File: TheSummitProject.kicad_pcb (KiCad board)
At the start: 4 copper layers, 70 x 65 mm, 81 parts, among them IC1 STM32U5F7VJT6, J1 Cortex SWD, J4 Screen FPC, J5 Micro_SD_Card_Det1, Q1 NMOS, SW1 SW_SPDT, SW2 PWR_BTN, U1 NPM1300-CAAA-R, U2 USBLC6-2SC6, U3 USBLC6-2SC6, Y1 16Mhz, Y2 32.768Khz

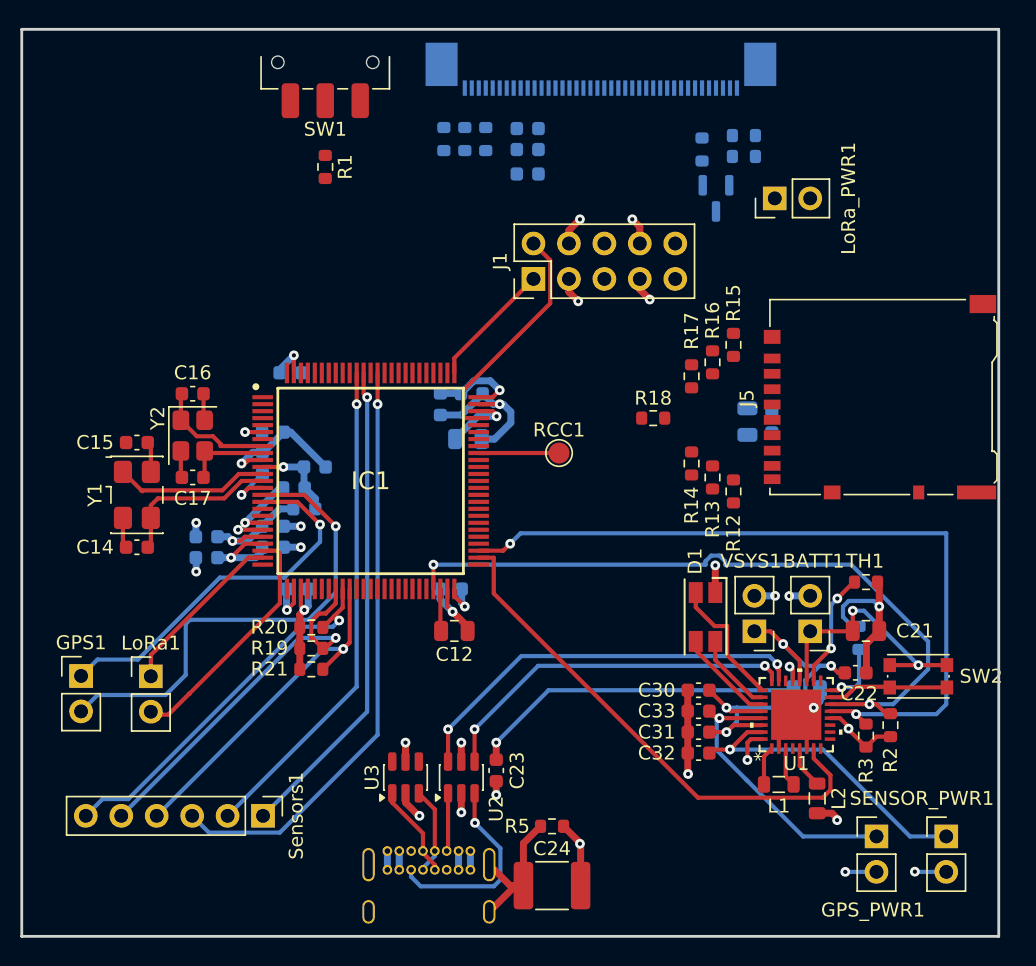
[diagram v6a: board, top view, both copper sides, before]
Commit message: added 90% pcb traces
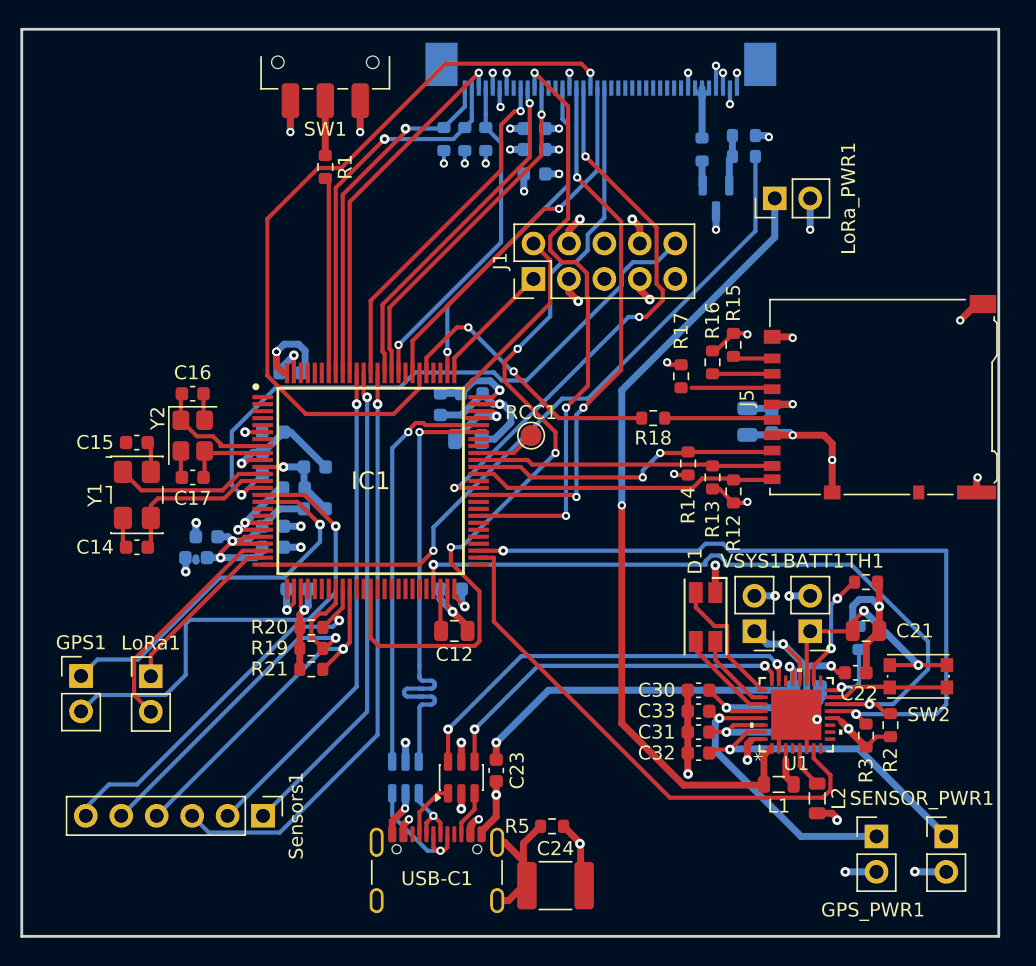
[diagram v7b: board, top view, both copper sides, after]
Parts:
- U3: moved to B.Cu
- USB-C1: footprint Connector_USB:USB_C_Receptacle_GCT_USB4085 -> Connector_USB:USB_C_Receptacle_GCT_USB4105-xx-A_16P_TopMnt_Horizontal; moved to F.Cu
- moved USB-C1 3.45 mm to (154.8, 129.5), turned to 0 degrees
- moved RCC1 2.36 mm to (161.5, 97.2)
- moved C10 0.75 mm to (137.5, 106.0)
- moved FB1 0.75 mm to (146.0, 102.5)
- moved R17 0.75 mm to (172.2, 93.0)
- moved C25 0.50 mm to (161.8, 76.8)
- moved C26 0.50 mm to (161.8, 75.2)
- moved C27 0.50 mm to (161.8, 78.5)
- moved C24 0.25 mm to (163.2, 129.5)
- moved R14 0.25 mm to (172.8, 99.2)
- turned R18 to 180 degrees
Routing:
- net +3.3V_DP_LORA: track 2.81 -> 67.7 mm, vias 0 -> 11
- net LCD_D4: track 0.00 -> 60.8 mm, vias 0 -> 3
- net LCD_D2: track 0.00 -> 54.3 mm, vias 0 -> 1
- net LCD_PWM: track 0.00 -> 51.5 mm, vias 0 -> 1
- net /MCU/NRST: track 3.84 -> 47.0 mm
- net LCD_RS: track 0.00 -> 43.0 mm, vias 0 -> 3
- net LCD_D1: track 0.00 -> 39.8 mm, vias 0 -> 3
- net LCD_D0: track 0.00 -> 39.0 mm, vias 0 -> 3
- net Net-(IC1-USB_OTG_HS_DM): track 0.00 -> 33.6 mm, vias 0 -> 1
- net Net-(IC1-USB_OTG_HS_DP): track 0.00 -> 29.5 mm, vias 0 -> 1
- net CTP_SDA: track 0.00 -> 27.3 mm, vias 0 -> 1
- net LCD_D3: track 0.00 -> 26.5 mm, vias 0 -> 1
- net CTP_RST: track 0.00 -> 26.4 mm, vias 0 -> 1
- net CTP_SCL: track 0.00 -> 25.6 mm, vias 0 -> 1
- net LCD_NE1: track 0.00 -> 25.1 mm, vias 0 -> 1
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
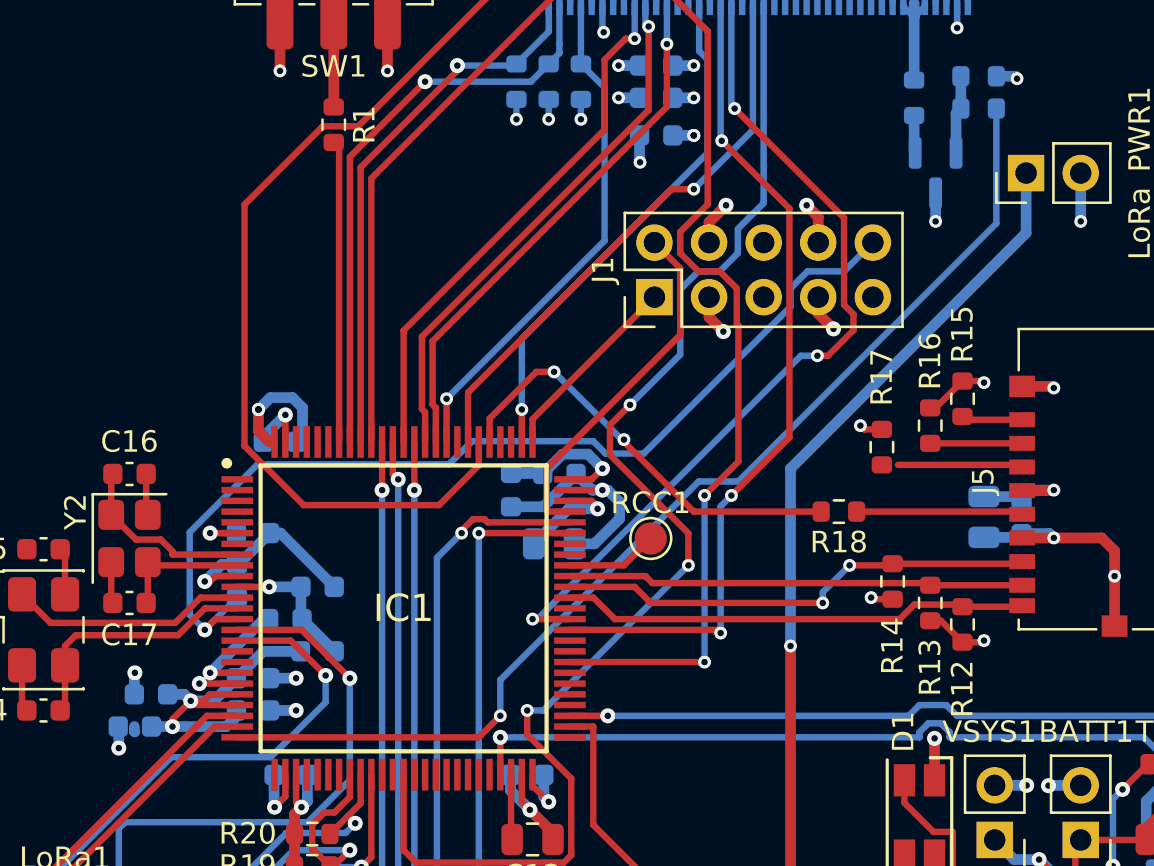
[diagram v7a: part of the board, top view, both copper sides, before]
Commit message: added 90% pcb traces
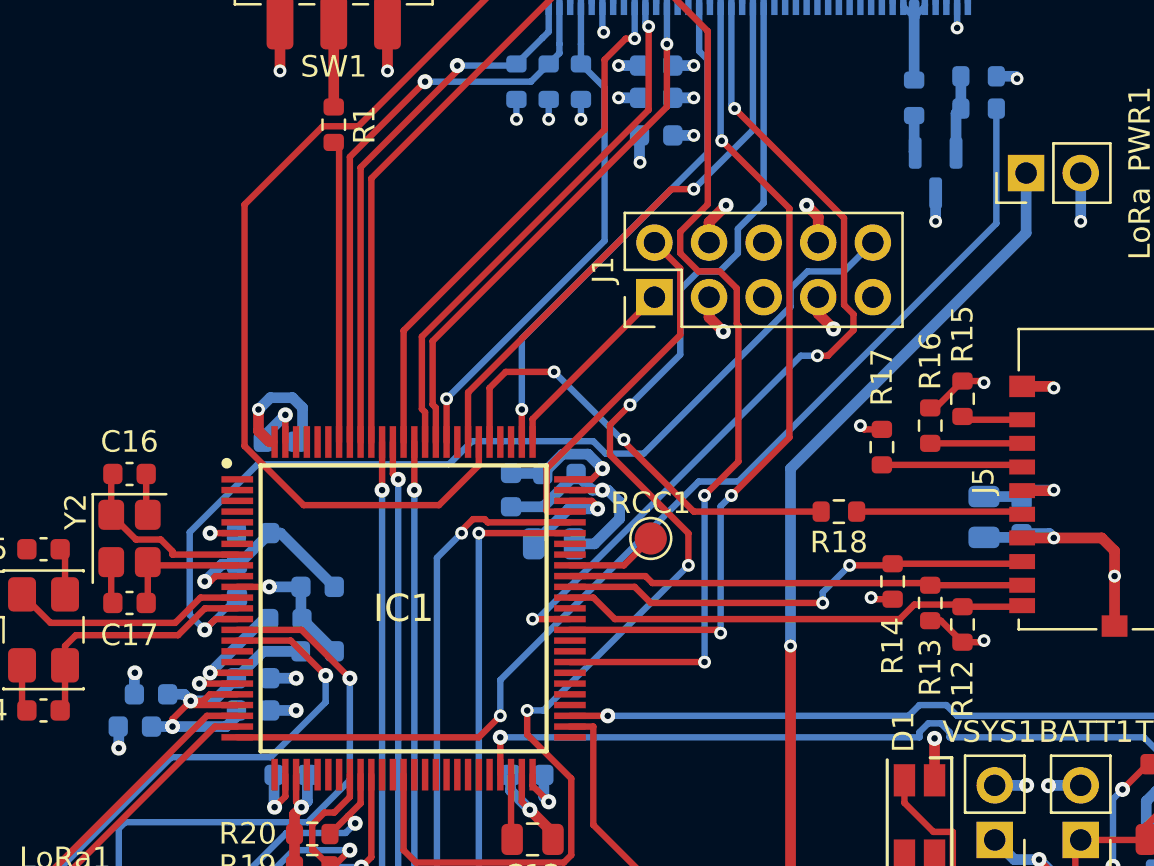
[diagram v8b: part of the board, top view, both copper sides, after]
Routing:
- net SD_CK: track 20.2 -> 21.0 mm
- net SD_CMD: track 5.82 -> 6.57 mm
- net GND: track 132.2 -> 132.0 mm, vias 42 -> 41
- net +3.3V: vias 21 -> 19
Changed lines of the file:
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@@
 	)
 	(via
-		(at 143.25 91.25)
-		(size 0.6)
-		(drill 0.3)
-		(layers "F.Cu" "B.Cu")
-		(net "+3.3V")
-	)
-	(via
 		(at 165 81.75)
 		(size 0.7)
@@
 	)
 	(via
-		(at 143.25 91.25)
-		(size 0.6)
-		(drill 0.3)
-		(layers "F.Cu" "B.Cu")
-		(net "+3.3V")
-	)
-	(via
 		(at 174.7 106.55)
 		(size 0.7)
@@
 	)
 	(via
-		(at 163.5 78.5)
-		(size 0.6)
-		(drill 0.3)
-		(layers "F.Cu" "B.Cu")
-		(net "GND")
-	)
-	(via
 		(at 181.5 82.5)
 		(size 0.6)
@@
 	)
 	(segment
-		(start 137.475 106.225)
-		(end 137.5 106.25)
-		(width 0.5)
-		(layer "B.Cu")
-		(net "GND")
-	)
-	(segment
 		(start 160.05 96.331371)
 		(end 158.881371 97.5)
@@
 	)
 	(segment
-		(start 137.475 106)
-		(end 137.475 106.225)
-		(width 0.5)
-		(layer "B.Cu")
-		(net "GND")
-	)
-	(segment
 		(start 152.5 122.8875)
 		(end 152.5 123.939796)
@@
 	)
 	(segment
-		(start 173 93.825)
-		(end 178.675 93.825)
+		(start 178.675 93.825)
+		(end 172.25 93.825)
 		(width 0.3)
 		(layer "F.Cu")
@@
 	)
 	(segment
-		(start 178.675 93.825)
-		(end 178.775 93.925)
+		(start 178.775 93.925)
+		(end 178.675 93.825)
 		(width 0.3)
 		(layer "F.Cu")
@@
 	)
 	(segment
-		(start 157 89.5)
-		(end 156.1745 89.5)
+		(start 163.5 96)
+		(end 169.425 96)
 		(width 0.3)
 		(layer "F.Cu")
@@
 	)
 	(segment
-		(start 163.5 96)
-		(end 169.425 96)
+		(start 154 90.25)
+		(end 154 92.762)
 		(width 0.3)
 		(layer "F.Cu")
@@
 	)
 	(segment
-		(start 154 91.6745)
-		(end 154 92.762)
+		(start 160.25 92.75)
+		(end 163.5 96)
 		(width 0.3)
 		(layer "F.Cu")
@@
 	)
 	(segment
-		(start 156.1745 89.5)
-		(end 154 91.6745)
+		(start 157 89.5)
+		(end 154.75 89.5)
 		(width 0.3)
 		(layer "F.Cu")
@@
 	)
 	(segment
-		(start 160.25 92.75)
-		(end 163.5 96)
+		(start 154.75 89.5)
+		(end 154 90.25)
 		(width 0.3)
 		(layer "F.Cu")
